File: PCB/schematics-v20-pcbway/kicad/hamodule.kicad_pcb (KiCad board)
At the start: 2 copper layers, 78.4 x 84.3 mm, 104 parts, among them J1 GND|5V, J10 USB_C_Receptacle_USB2.0, J11 2604-1104, J12 2604-1104, J13 EspSense, J2 Conn_01x02_Male, J3 2604-1102, J4 USB | PS, J5 Conn_01x02_Male, J6 GND|3.3V, J7 Conn_01x02_Male, J8 Current Jumper, J9 EspRelays, K1 AQG12205, K2 AQG12205, K3 AQG12205, K4 AQG12205, Q1 SS8050, Q2 SS8050, SW1 Switch, SW2 Switch, U1 LD1117AV33, U2 ESP32-WROOM-32E, U3 CP2102N-A01-GQFN28, U4 ULN2003A, U5 LDA210-PDIP, U6 LDA210-PDIP, U7 SHT4x

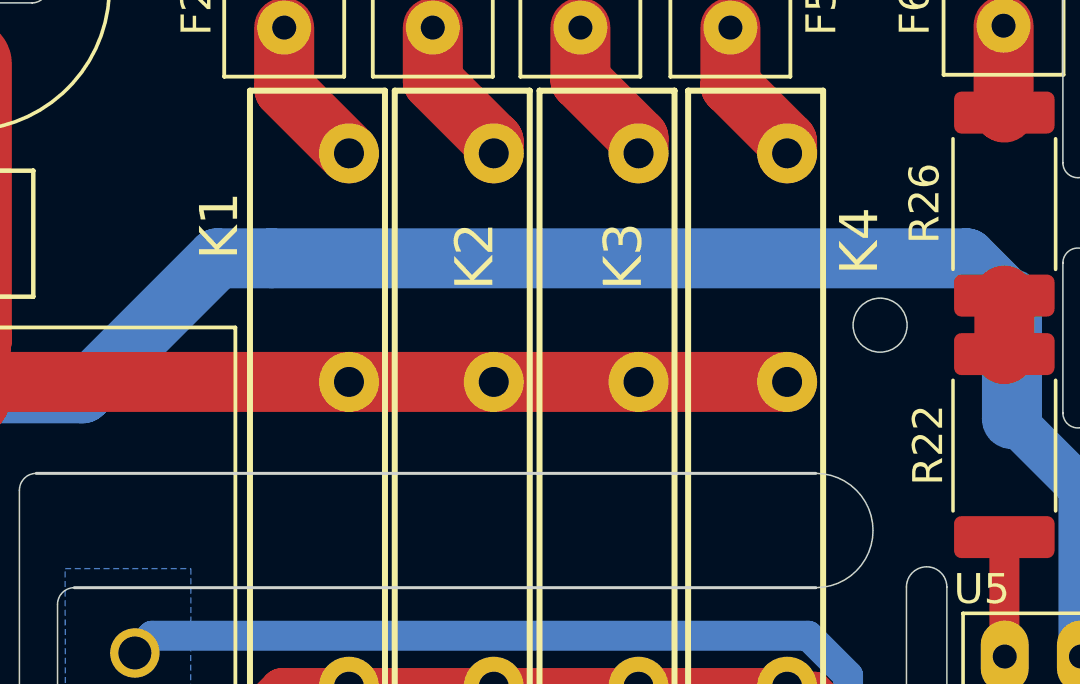
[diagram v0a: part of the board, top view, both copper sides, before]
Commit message: [V20] fixing net classes and removing exceptions. Nothing changed in the PCB itself
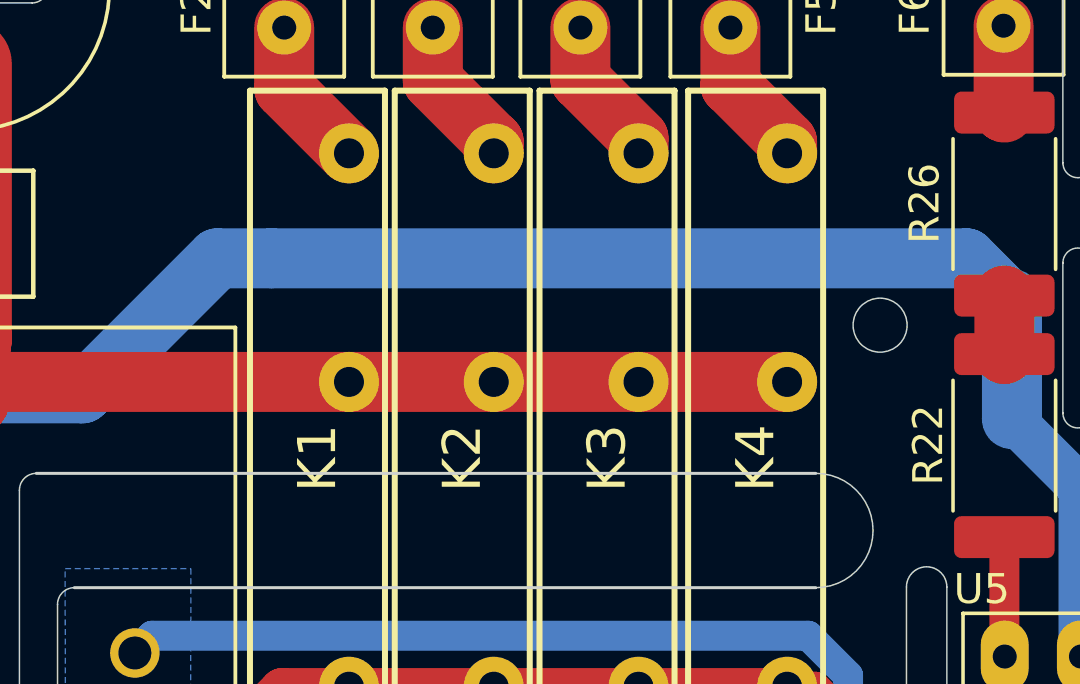
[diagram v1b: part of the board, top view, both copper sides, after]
